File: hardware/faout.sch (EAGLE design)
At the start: 124 parts, among them IC1 MT48LC64M4A2, Q1 12MHz, Q2 ASFL, U1 93C46B, U10 OPA2277UA/2K5E4, U11 DAC8811DGK, U12 MCP1700T-2502E/TT, U13 AD7980ARMZ, U14 ADR435ARZ, U15 AD8627AKSZ-R2, U2 LTC3419EMS, U3 FLASH-SPI-25XXSMD1, U4 6SLX9TQG144, U5 AD8220ARMZ, U6 REF102AU, U7 OPA2277UA/2K5E4, U8 DAC8811DGK, U9 REF102AU

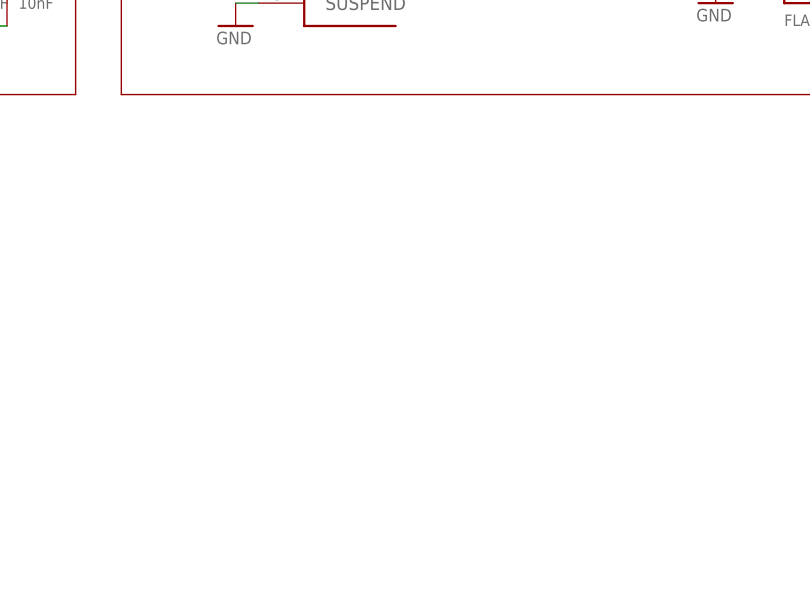
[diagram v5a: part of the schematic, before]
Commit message: Added 7-segment display.
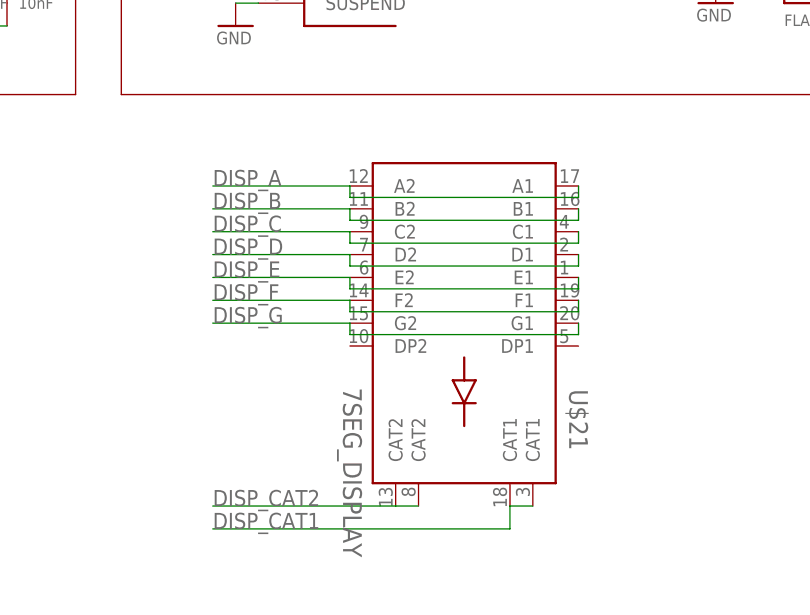
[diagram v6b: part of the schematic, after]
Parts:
- added U$21: 7SEG_DISPLAY, faout:7SEG_DISPLAY
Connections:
- new net DISP_A: U$21.A1, U$21.A2
- new net DISP_B: U$21.B1, U$21.B2
- new net DISP_C: U$21.C1, U$21.C2
- new net DISP_CAT1: U$21.CAT1@1, U$21.CAT1@2
- new net DISP_CAT2: U$21.CAT2@1, U$21.CAT2@2
- new net DISP_D: U$21.D1, U$21.D2
- new net DISP_E: U$21.E1, U$21.E2
- new net DISP_F: U$21.F1, U$21.F2
- new net DISP_G: U$21.G1, U$21.G2
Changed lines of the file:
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@@
 <part name="JP3" library="pinhead" deviceset="PINHD-1X2" device=""/>
 <part name="GND_PWR62" library="faout" deviceset="GND" device=""/>
+<part name="U$21" library="faout" deviceset="7SEG_DISPLAY" device=""/>
 </parts>
 <sheets>
@@
 <instance part="JP3" gate="G$1" x="55.88" y="-139.7"/>
 <instance part="GND_PWR62" gate="A" x="53.34" y="-142.24"/>
+<instance part="U$21" gate="G$1" x="182.88" y="-320.04" rot="R270"/>
 </instances>
 <busses>
@@
 </segment>
 </net>
+<net name="DISP_A" class="0">
+<segment>
+<pinref part="U$21" gate="G$1" pin="A1"/>
+<wire x1="195.58" y1="-307.34" x2="195.58" y2="-308.61" width="0.1524" layer="91"/>
+<wire x1="195.58" y1="-308.61" x2="170.18" y2="-308.61" width="0.1524" layer="91"/>
+<pinref part="U$21" gate="G$1" pin="A2"/>
+<wire x1="170.18" y1="-308.61" x2="170.18" y2="-307.34" width="0.1524" layer="91"/>
+<wire x1="154.94" y1="-307.34" x2="170.18" y2="-307.34" width="0.1524" layer="91"/>
+<label x="154.94" y="-307.34" size="1.778" layer="95"/>
+</segment>
+</net>
+<net name="DISP_B" class="0">
+<segment>
+<pinref part="U$21" gate="G$1" pin="B2"/>
+<wire x1="170.18" y1="-309.88" x2="170.18" y2="-311.15" width="0.1524" layer="91"/>
+<wire x1="170.18" y1="-311.15" x2="195.58" y2="-311.15" width="0.1524" layer="91"/>
+<pinref part="U$21" gate="G$1" pin="B1"/>
+<wire x1="195.58" y1="-311.15" x2="195.58" y2="-309.88" width="0.1524" layer="91"/>
+<wire x1="170.18" y1="-309.88" x2="154.94" y2="-309.88" width="0.1524" layer="91"/>
+<label x="154.94" y="-309.88" size="1.778" layer="95"/>
+</segment>
+</net>
+<net name="DISP_C" class="0">
+<segment>
+<pinref part="U$21" gate="G$1" pin="C1"/>
+<wire x1="195.58" y1="-312.42" x2="195.58" y2="-313.69" width="0.1524" layer="91"/>
+<wire x1="195.58" y1="-313.69" x2="170.18" y2="-313.69" width="0.1524" layer="91"/>
+<pinref part="U$21" gate="G$1" pin="C2"/>
+<wire x1="170.18" y1="-313.69" x2="170.18" y2="-312.42" width="0.1524" layer="91"/>
+<wire x1="170.18" y1="-312.42" x2="154.94" y2="-312.42" width="0.1524" layer="91"/>
+<label x="154.94" y="-312.42" size="1.778" layer="95"/>
+</segment>
+</net>
+<net name="DISP_D" class="0">
+<segment>
+<pinref part="U$21" gate="G$1" pin="D2"/>
+<wire x1="170.18" y1="-314.96" x2="170.18" y2="-316.23" width="0.1524" layer="91"/>
+<wire x1="170.18" y1="-316.23" x2="195.58" y2="-316.23" width="0.1524" layer="91"/>
+<pinref part="U$21" gate="G$1" pin="D1"/>
+<wire x1="195.58" y1="-316.23" x2="195.58" y2="-314.96" width="0.1524" layer="91"/>
+<wire x1="170.18" y1="-314.96" x2="154.94" y2="-314.96" width="0.1524" layer="91"/>
+<label x="154.94" y="-314.96" size="1.778" layer="95"/>
+</segment>
+</net>
+<net name="DISP_E" class="0">
+<segment>
+<pinref part="U$21" gate="G$1" pin="E1"/>
+<wire x1="195.58" y1="-317.5" x2="195.58" y2="-318.77" width="0.1524" layer="91"/>
+<wire x1="195.58" y1="-318.77" x2="170.18" y2="-318.77" width="0.1524" layer="91"/>
+<pinref part="U$21" gate="G$1" pin="E2"/>
+<wire x1="170.18" y1="-318.77" x2="170.18" y2="-317.5" width="0.1524" layer="91"/>
+<wire x1="170.18" y1="-317.5" x2="154.94" y2="-317.5" width="0.1524" layer="91"/>
+<label x="154.94" y="-317.5" size="1.778" layer="95"/>
+</segment>
+</net>
+<net name="DISP_F" class="0">
+<segment>
+<pinref part="U$21" gate="G$1" pin="F2"/>
+<wire x1="170.18" y1="-320.04" x2="170.18" y2="-321.31" width="0.1524" layer="91"/>
+<wire x1="170.18" y1="-321.31" x2="195.58" y2="-321.31" width="0.1524" layer="91"/>
+<pinref part="U$21" gate="G$1" pin="F1"/>
+<wire x1="195.58" y1="-321.31" x2="195.58" y2="-320.04" width="0.1524" layer="91"/>
+<wire x1="170.18" y1="-320.04" x2="154.94" y2="-320.04" width="0.1524" layer="91"/>
+<label x="154.94" y="-320.04" size="1.778" layer="95"/>
+</segment>
+</net>
+<net name="DISP_G" class="0">
+<segment>
+<pinref part="U$21" gate="G$1" pin="G2"/>
+<wire x1="170.18" y1="-322.58" x2="170.18" y2="-323.85" width="0.1524" layer="91"/>
+<wire x1="170.18" y1="-323.85" x2="195.58" y2="-323.85" width="0.1524" layer="91"/>
+<pinref part="U$21" gate="G$1" pin="G1"/>
+<wire x1="195.58" y1="-323.85" x2="195.58" y2="-322.58" width="0.1524" layer="91"/>
+<wire x1="170.18" y1="-322.58" x2="154.94" y2="-322.58" width="0.1524" layer="91"/>
+<label x="154.94" y="-322.58" size="1.778" layer="95"/>
+</segment>
+</net>
+<net name="DISP_CAT2" class="0">
+<segment>
+<pinref part="U$21" gate="G$1" pin="CAT2@1"/>
+<pinref part="U$21" gate="G$1" pin="CAT2@2"/>
+<wire x1="177.8" y1="-342.9" x2="175.26" y2="-342.9" width="0.1524" layer="91"/>
+<wire x1="175.26" y1="-342.9" x2="154.94" y2="-342.9" width="0.1524" layer="91"/>
+<label x="154.94" y="-342.9" size="1.778" layer="95"/>
+</segment>
+</net>
+<net name="DISP_CAT1" class="0">
+<segment>
+<pinref part="U$21" gate="G$1" pin="CAT1@1"/>
+<pinref part="U$21" gate="G$1" pin="CAT1@2"/>
+<wire x1="190.5" y1="-342.9" x2="187.96" y2="-342.9" width="0.1524" layer="91"/>
+<wire x1="187.96" y1="-342.9" x2="187.96" y2="-345.44" width="0.1524" layer="91"/>
+<wire x1="187.96" y1="-345.44" x2="154.94" y2="-345.44" width="0.1524" layer="91"/>
+<label x="154.94" y="-345.44" size="1.778" layer="95"/>
+</segment>
+</net>

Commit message: Finished User IO, create new power supply.
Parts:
- removed R10, R12, R9: 1K5 1%, faout:R_EU0603
- removed R11: 6K8 1%, faout:R_EU0603
- removed U$21: 7SEG_DISPLAY, faout:7SEG_DISPLAY
- added C72, C73, C74: 4.7uF, faout:C_EU0603
- added DISP1: 7SEG_DISPLAY, faout:7SEG_DISPLAY
- added JP4: (no value), pinhead:PINHD-1X6
- added LED3, LED4, LED5: (no value), led:LEDSML0805
- added Q3: MUN2214T1, transistor-npn:MUN2214T1
- added Q4: ASFL, crystal:ASFL
- added R21, R22, R23: 10k, faout:R_EU0603
- added R24, R25, R26, R27, R28: 300, faout:R_EU0603
- added R29, R30: 7.47k, faout:R_EU0603
- added R31: 134k, faout:R_EU0603
- added R32, R33: 2k, faout:R_EU0603
- added SW1, SW2, SW3: SMD_TACT_SWITCH, faout:SMD_TACT_SWITCH
- added U16: LM3671MF-3.3, faout:LM3671MF-3.3
- C1, C19, C20, C28, C29, C30, C31, C34, C36, C38, C4, C40, C41, C42, C43, C46, C48, C49, C6: OC_FARNELL (none) -> 1833803
- C10, C11, C13, C14, C15, C16, C5, C51, C53, C61, C62, C66, C67, C68, C7, C8, C9: OC_FARNELL (none) -> 1740621
- C12: value 10uF/10V -> 4.7uF; device faout:C_EU0805 -> faout:C_EU0603; OC_FARNELL (none) -> 1833803
- C17, C18, C25, C26, C27, C32, C33, C37, C39, C45, C47: OC_FARNELL (none) -> 1867949
- C22, C23: value 22uF/6V3 -> 4.7uF; device faout:C_EU0805 -> faout:C_EU0603; OC_FARNELL (none) -> 1833803
- C50: value 1uF? -> 100nF; OC_FARNELL (none) -> 1740621
- C54: value 1uF -> 1uF?
- C55: value 1uF -> 100nF; OC_FARNELL (none) -> 1740621
- C56: value 100nF -> 114pF
- C57: value 20pF -> 11.4pF
- C58: value 20pF -> 100nF; OC_FARNELL (none) -> 1740621
- C59, C60: value 1nF -> 20pF
- C63, C64: value 100nF -> 1nF
- C65: value 22uF -> 100nF; device resistor:C-EUC1206 -> faout:C_EU0603; OC_FARNELL (none) -> 1740621
- C69: value 100nF -> 1uF
- C70: value 114pF -> 22uF; device faout:C_EU0603 -> resistor:C-EUC1206
- C71: value 11.4pF -> 1uF
- IC1: value MT48LC64M4A2 -> (none); device faout:MT48LC64M4A2 -> ftdichip-3:FT2232HL
- IC2: value (none) -> MT48LC8M16A2; device ftdichip-3:FT2232HL -> faout:MT48LC8M16A2
- JP1: device pinhead:PINHD-1X6 -> pinhead:PINHD-1X2
- JP2: device pinhead:PINHD-1X2 -> pinhead:PINHD-1X6
- L3: value 3.3uH -> (none); device Bogdan_Commons:L_VLS3015 -> faout:R_EU0603
- L4: value 3.3uH -> 2.2uH; device Bogdan_Commons:L_VLS3015 -> rcl:L-EUL5038P; OC_FARNELL (none) -> 2145272
- L5: value (none) -> 2.2uH; device faout:R_EU0603 -> rcl:L-EUL5038P; OC_FARNELL (none) -> 2145272
- Q2: value ASFL -> MUN2214T1; device crystal:ASFL -> transistor-npn:MUN2214T1; OC_FARNELL (none) -> 2317629
- R14, R15: value 300 -> 100
- R16, R17: value 2k -> 100
- R18, R19: value 7.47k -> 100
- R20: value 134k -> 100
- U10: value OPA2277UA/2K5E4 -> ADR435ARZ; device faout:OPA2277UA/2K5E4 -> faout:ADR435ARZ
- U11: value DAC8811DGK -> AD8627AKSZ-R2; device faout:DAC8811DGK -> faout:AD8627AKSZ-R2
- U12: value MCP1700T-2502E/TT -> OPA2277UA/2K5E4; device faout:MCP1700T-2502E/TT -> faout:OPA2277UA/2K5E4
- U13: value AD7980ARMZ -> OPA2277UA/2K5E4; device faout:AD7980ARMZ -> faout:OPA2277UA/2K5E4
- U14: value ADR435ARZ -> MCP1700T-2502E/TT; device faout:ADR435ARZ -> faout:MCP1700T-2502E/TT
- U15: value AD8627AKSZ-R2 -> AD7980ARMZ; device faout:AD8627AKSZ-R2 -> faout:AD7980ARMZ
- U2: value LTC3419EMS -> LM3671MF-1.2; device Bogdan_Commons:LTC3419EMS -> faout:LM3671MF-1.2
- U7: value OPA2277UA/2K5E4 -> DAC8811DGK; device faout:OPA2277UA/2K5E4 -> faout:DAC8811DGK
- U8: value DAC8811DGK -> REF102AU; device faout:DAC8811DGK -> faout:REF102AU
- U9: value REF102AU -> DAC8811DGK; device faout:REF102AU -> faout:DAC8811DGK
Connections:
- removed net DISP_CAT2: U$21.CAT2@1, U$21.CAT2@2
- removed net FB_1V2: R10.P$2, R12.P$1, U2.VFB2
- removed net FB_3V3: R11.P$1, R9.P$2, U2.VFB1
- removed net LED_1: LED1.A, U4B0.IO_L66P_SCP1_0
- removed net LED_2: LED2.A, U4B0.IO_L66N_SCP0_0
- removed net RAM_A12: IC1G$1.A12, U4B3.IO_L1N_VREF_3
- removed net SW_1V2: L4.1, U2.SW2
- removed net SW_3V3: L3.1, U2.SW1
- new net BUTTON1: SW1.1, U4B2.IO_L12N_D2_MISO3_2
- new net BUTTON2: SW2.1, U4B2.IO_L12P_D1_MISO2_2
- new net BUTTON3: SW3.1, U4B2.IO_L2N_CMPMOSI_2
- new net DISP_EN1: Q3.B, U4B2.IO_L14P_D11_2
- new net DISP_EN2: Q2.B, U4B2.IO_L13N_D10_2
- new net DISP_INT_A: DISP1.A1, DISP1.A2, R14.P$1
- new net DISP_INT_B: DISP1.B1, DISP1.B2, R15.P$1
- new net DISP_INT_C: DISP1.C1, DISP1.C2, R16.P$1
- new net DISP_INT_D: DISP1.D1, DISP1.D2, R17.P$1
- new net DISP_INT_E: DISP1.E1, DISP1.E2, R18.P$1
- new net DISP_INT_F: DISP1.F1, DISP1.F2, R19.P$1
- new net DISP_INT_G: DISP1.G1, DISP1.G2, R20.P$1
- new net JP_1: JP4.1, U4B1.IO_L43N_GCLK4_1
- new net JP_2: JP4.2, U4B1.IO_L45P_1
- new net JP_3: JP4.3, U4B1.IO_L45N_1
- new net JP_4: JP4.4, U4B1.IO_L46P_1
- new net LED1: LED1.A, U4B1.IO_L46N_1
- new net LED2: LED2.A, U4B1.IO_L47P_1
- new net LED3: LED3.A, U4B1.IO_L47N_1
- new net LED_4: LED4.A, U4B0.IO_L66P_SCP1_0
- new net LED_5: LED5.A, U4B0.IO_L66N_SCP0_0
- new net N$17: DISP1.CAT2@1, DISP1.CAT2@2, Q2.C
- new net N$18: R21.P$1, SW1.2
- new net N$19: R22.P$1, SW2.2
- new net N$20: R23.P$1, SW3.2
- new net N$21: LED1.C, R24.P$2
- new net N$22: LED2.C, R25.P$2
- new net N$23: LED3.C, R26.P$2
- new net N$24: L4.1, U16.SW
- new net N$25: L5.1, U2.SW
- net !DAC1_CS: now also U7.!CS; no longer U8.!CS
- net !DAC2_CS: now also U9.!CS; no longer U11.!CS
- net !RAM_CAS: now also IC2G$1.!CAS; no longer IC1G$1.!CAS
- net !RAM_RAS: now also IC2G$1.!RAS; no longer IC1G$1.!RAS
- net !RAM_WE: now also IC2G$1.!WE; no longer IC1G$1.!WE
- net !USB_OE: now also IC1.ACBUS6; no longer IC2.ACBUS6
- net !USB_RD: now also IC1.ACBUS2; no longer IC2.ACBUS2
- net !USB_RESET: now also IC1.-RESET, JP1.1; no longer IC2.-RESET, JP3.1
- net !USB_RXF: now also IC1.ACBUS0; no longer IC2.ACBUS0
- net !USB_TXE: now also IC1.ACBUS1; no longer IC2.ACBUS1
- net !USB_WR: now also IC1.ACBUS3; no longer IC2.ACBUS3
- net 1V2: now also C73.P$1, C74.P$1, L5.2, U2.FB; no longer C23.P$1, L4.2, R12.P$2
- net 1V8: now also IC1.VCORE@1, IC1.VCORE@2, IC1.VCORE@3, IC1.VREGOUT; no longer IC2.VCORE@1, IC2.VCORE@2, IC2.VCORE@3, IC2.VREGOUT
- net 2V5: now also C69.P$1, U14.VOUT, U15.VDD; no longer C55.P$1, U12.VOUT, U13.VDD
- net 3V3: now also C23.P$1, C72.P$1, IC1.ACBUS4, IC1.VCCIO@1, IC1.VCCIO@2, IC1.VCCIO@3, IC1.VCCIO@4, IC1.VREGIN, IC2P.VDD@1, IC2P.VDD@2, IC2P.VDD@3, IC2P.VDDQ@1, IC2P.VDDQ@2, IC2P.VDDQ@3, IC2P.VDDQ@4, JP2.6, JP4.6, L3.P$1, L4.2, Q4.OE, Q4.VCC, R21.P$2, R22.P$2, R23.P$2, U16.FB, U2.EN; no longer C22.P$1, IC1P.VDD@1, IC1P.VDD@2, IC1P.VDD@3, IC1P.VDDQ@1, IC1P.VDDQ@2, IC1P.VDDQ@3, IC1P.VDDQ@4, IC2.ACBUS4, IC2.VCCIO@1, IC2.VCCIO@2, IC2.VCCIO@3, IC2.VCCIO@4, IC2.VREGIN, JP1.6, L1.P$1, L3.2, Q2.OE, Q2.VCC, R11.P$2, U2.RUN2
- net 5V0: now also C22.P$1, U16.EN, U16.VIN; no longer U2.MODE, U2.RUN1
- net A+12V: now also C50.P$1, C58.P$1, C65.P$1, C67.P$1, U10.VIN, U11.V+, U12.V+, U13.V+; no longer C56.P$1, C63.P$1, C66.P$1, C68.P$1, U10.V+, U14.VIN, U15.V+, U7.V+
- net A+3V3: now also C55.P$1, C71.P$1, U14.VIN, U15.VIO, U7.VDD, U8.V+, U9.VDD; no longer C50.P$1, C51.P$1, U11.VDD, U12.VIN, U13.VIO, U8.VDD, U9.V+
- net A-12V: now also C51.P$2, C66.P$2, C68.P$2, U11.V-, U12.V-, U13.V-; no longer C64.P$2, C67.P$2, C69.P$2, U10.V-, U15.V-, U7.V-
- net ADC1_CNV: now also U15.CNV; no longer U13.CNV
- net ADC1_REF: now also C70.1, U10.VOUT, U15.REF; no longer C65.1, U13.REF, U14.VOUT
- net ADC1_SCK: now also U15.SCK; no longer U13.SCK
- net ADC1_SDI: now also U15.SDI; no longer U13.SDI
- net ADC1_SDO: now also U15.SDO; no longer U13.SDO
- net CLK_IN: now also Q4.FO; no longer Q2.FO
- net DAC1_CLK: now also U7.CLK; no longer U8.CLK
- net DAC1_IOUT: now also C59.P$2, U13.-IN_A, U7.IOUT; no longer C57.P$2, U7.-IN_A, U8.IOUT
- net DAC1_SDI: now also U7.SDI; no longer U8.SDI
- net DAC1_VOUT: now also C59.P$1, U13.OUT_A, U7.RFB; no longer C57.P$1, U7.OUT_A, U8.RFB
- net DAC1_VREF: now also C52.P$2, C63.P$2, U13.OUT_B, U7.VREF; no longer C50.P$2, C59.P$2, U7.OUT_B, U8.VREF
- net DAC1_VREFOUT: now also C63.P$1, R32.P$2, U13.-IN_B; no longer C59.P$1, R16.P$2, U7.-IN_B
- net DAC2_CLK: now also U9.CLK; no longer U11.CLK
- net DAC2_IOUT: now also C60.P$2, U12.-IN_A, U9.IOUT; no longer C58.P$2, U10.-IN_A, U11.IOUT
- net DAC2_SDI: now also U9.SDI; no longer U11.SDI
- net DAC2_VOUT: now also C60.P$1, U12.OUT_A, U9.RFB; no longer C58.P$1, U10.OUT_A, U11.RFB
- net DAC2_VREF: now also C54.P$2, C64.P$2, U12.OUT_B, U8.COM, U9.VREF; no longer C52.P$2, C60.P$2, U10.OUT_B, U11.VREF, U9.COM
- net DAC2_VREFOUT: now also C64.P$1, R33.P$2, U12.-IN_B; no longer C60.P$1, R17.P$2, U10.-IN_B
- net DISP_A: now also R14.P$2, U4B2.IO_L30N_GCLK0_USERCCLK_2; no longer U$21.A1, U$21.A2
- net DISP_B: now also R15.P$2, U4B2.IO_L30P_GCLK1_D13_2; no longer U$21.B1, U$21.B2
- net DISP_C: now also R16.P$2, U4B2.IO_L48P_D7_2; no longer U$21.C1, U$21.C2
- net DISP_CAT1: now also DISP1.CAT1@1, DISP1.CAT1@2, Q3.C; no longer U$21.CAT1@1, U$21.CAT1@2
- net DISP_D: now also R17.P$2, U4B2.IO_L31N_GCLK30_D15_2; no longer U$21.D1, U$21.D2
- net DISP_E: now also R18.P$2, U4B2.IO_L48N_RDWR_B_VREF_2; no longer U$21.E1, U$21.E2
- net DISP_F: now also R19.P$2, U4B2.IO_L31P_GCLK31_D14_2; no longer U$21.F1, U$21.F2
- net DISP_G: now also R20.P$2, U4B2.IO_L14N_D12_2; no longer U$21.G1, U$21.G2
- net EECS: now also IC1.EECS; no longer IC2.EECS
- net EEDATA: now also IC1.EEDATA; no longer IC2.EEDATA
- net EESK: now also IC1.EESK; no longer IC2.EESK
- net GND: now also C50.P$2, C51.P$1, C57.P$2, C58.P$2, C65.P$2, C66.P$1, C67.P$2, C68.P$1, C69.P$2, C70.2, C72.P$2, C73.P$2, C74.P$2, IC1.AGND, IC1.GND@1, IC1.GND@2, IC1.GND@3, IC1.GND@4, IC1.GND@5, IC1.GND@6, IC1.GND@7, IC1.GND@8, IC1.TEST, IC2P.VSS@1, IC2P.VSS@2, IC2P.VSS@3, IC2P.VSSQ@1, IC2P.VSSQ@2, IC2P.VSSQ@3, IC2P.VSSQ@4, JP1.2, JP2.1, JP4.5, L1.P$2, Q2.E, Q3.E, Q4.GND, R24.P$1, R25.P$1, R26.P$1, R27.P$1, R28.P$1, R30.P$1, SW1.3, SW1.4, SW2.3, SW2.4, SW3.3, SW3.4, U10.GND, U12.+IN_A, U12.+IN_B, U13.+IN_A, U13.+IN_B, U15.GND, U15.IN-, U16.GND, U2.GND, U7.GND, U9.GND; no longer C51.P$2, C54.P$2, C56.P$2, C63.P$2, C64.P$1, C65.2, C66.P$2, C67.P$1, C68.P$2, C69.P$1, IC1P.VSS@1, IC1P.VSS@2, IC1P.VSS@3, IC1P.VSSQ@1, IC1P.VSSQ@2, IC1P.VSSQ@3, IC1P.VSSQ@4, IC2.AGND, IC2.GND@1, IC2.GND@2, IC2.GND@3, IC2.GND@4, IC2.GND@5, IC2.GND@6, IC2.GND@7, IC2.GND@8, IC2.TEST, JP1.1, JP2.2, L5.P$2, Q2.GND, R10.P$1, R14.P$1, R15.P$1, R19.P$1, R9.P$1, U10.+IN_A, U10.+IN_B, U11.GND, U12.GND, U13.GND, U13.IN-, U2.GND@5, U2.GND@6, U7.+IN_A, U7.+IN_B, U8.GND
- net N$1: now also IC1.XTIN; no longer IC2.XTIN
- net N$10: now also R32.P$1; no longer R16.P$1
- net N$12: now also C56.P$1, U11.-IN, U11.OUT_A, U15.IN+; no longer C70.P$1, U13.IN+, U15.-IN, U15.OUT_A
- net N$13: now also R29.P$2; no longer R18.P$2
- net N$14: now also C56.P$2, R29.P$1, R30.P$2, R31.P$1; no longer C70.P$2, R18.P$1, R19.P$2, R20.P$1
- net N$15: now also C57.P$1, R31.P$2, U11.+IN; no longer C71.P$1, R20.P$2, U15.+IN
- net N$16: now also L1.P$1; no longer L5.P$1
- net N$2: now also IC1.XTOUT; no longer IC2.XTOUT
- net N$3: now also LED4.C, R27.P$2; no longer LED1.C, R14.P$2
- net N$4: now also LED5.C, R28.P$2; no longer LED2.C, R15.P$2
- net N$5: now also IC1.VPHY, L3.P$2; no longer IC2.VPHY, L2.P$2
- net N$7: now also IC1.VPLL, L2.P$2; no longer IC2.VPLL, L1.P$2
- net N$8: now also R33.P$1, U8.VOUT; no longer R17.P$1, U9.VOUT
- net RAM_A0: now also IC2G$1.A0; no longer IC1G$1.A0
- net RAM_A1: now also IC2G$1.A1; no longer IC1G$1.A1
- net RAM_A10: now also IC2G$1.A10; no longer IC1G$1.A10
- net RAM_A11: now also IC2G$1.A11; no longer IC1G$1.A11
- net RAM_A2: now also IC2G$1.A2; no longer IC1G$1.A2
- net RAM_A3: now also IC2G$1.A3; no longer IC1G$1.A3
- net RAM_A4: now also IC2G$1.A4; no longer IC1G$1.A4
- net RAM_A5: now also IC2G$1.A5; no longer IC1G$1.A5
- net RAM_A6: now also IC2G$1.A6; no longer IC1G$1.A6
- net RAM_A7: now also IC2G$1.A7; no longer IC1G$1.A7
- net RAM_A8: now also IC2G$1.A8; no longer IC1G$1.A8
- net RAM_A9: now also IC2G$1.A9; no longer IC1G$1.A9
- net RAM_BA0: now also IC2G$1.BA0; no longer IC1G$1.BA0
- net RAM_BA1: now also IC2G$1.BA1; no longer IC1G$1.BA1
- net RAM_CKE: now also IC2G$1.CKE; no longer IC1G$1.CKE
- net RAM_CLK: now also IC2G$1.CLK; no longer IC1G$1.CLK
- net RAM_CS: now also IC2G$1.\CS; no longer IC1G$1.\CS
- net RAM_DQ0: now also IC2G$1.DQ0; no longer IC1G$1.DQ0
- net RAM_DQ1: now also IC2G$1.DQ1; no longer IC1G$1.DQ1
- net RAM_DQ10: now also IC2G$1.DQ10; no longer IC1G$1.DQ10
- net RAM_DQ11: now also IC2G$1.DQ11; no longer IC1G$1.DQ11
- net RAM_DQ12: now also IC2G$1.DQ12; no longer IC1G$1.DQ12
- net RAM_DQ13: now also IC2G$1.DQ13; no longer IC1G$1.DQ13
- net RAM_DQ14: now also IC2G$1.DQ14; no longer IC1G$1.DQ14
- net RAM_DQ15: now also IC2G$1.DQ15; no longer IC1G$1.DQ15
- net RAM_DQ2: now also IC2G$1.DQ2; no longer IC1G$1.DQ2
- net RAM_DQ3: now also IC2G$1.DQ3; no longer IC1G$1.DQ3
- net RAM_DQ4: now also IC2G$1.DQ4; no longer IC1G$1.DQ4
- net RAM_DQ5: now also IC2G$1.DQ5; no longer IC1G$1.DQ5
- net RAM_DQ6: now also IC2G$1.DQ6; no longer IC1G$1.DQ6
- net RAM_DQ7: now also IC2G$1.DQ7; no longer IC1G$1.DQ7
- net RAM_DQ8: now also IC2G$1.DQ8; no longer IC1G$1.DQ8
- net RAM_DQ9: now also IC2G$1.DQ9; no longer IC1G$1.DQ9
- net RAM_DQMH: now also IC2G$1.DQMH; no longer IC1G$1.DQMH
- net RAM_DQML: now also IC2G$1.DQML; no longer IC1G$1.DQML
- net RESET: now also JP3.1; no longer JP2.1
- net TCK: now also IC1.BDBUS0, JP2.2; no longer IC2.BDBUS0, JP1.2
- net TDI: now also IC1.BDBUS1, JP2.3; no longer IC2.BDBUS1, JP1.3
- net TDO: now also IC1.BDBUS2, JP2.4; no longer IC2.BDBUS2, JP1.4
- net TMS: now also IC1.BDBUS3, JP2.5; no longer IC2.BDBUS3, JP1.5
- net USB_CLKOUT: now also IC1.ACBUS5; no longer IC2.ACBUS5
- net USB_D0: now also IC1.ADBUS0; no longer IC2.ADBUS0
- net USB_D1: now also IC1.ADBUS1; no longer IC2.ADBUS1
- net USB_D2: now also IC1.ADBUS2; no longer IC2.ADBUS2
- net USB_D3: now also IC1.ADBUS3; no longer IC2.ADBUS3
- net USB_D4: now also IC1.ADBUS4; no longer IC2.ADBUS4
- net USB_D5: now also IC1.ADBUS5; no longer IC2.ADBUS5
- net USB_D6: now also IC1.ADBUS6; no longer IC2.ADBUS6
- net USB_D7: now also IC1.ADBUS7; no longer IC2.ADBUS7
- net USB_DM: now also IC1.D-; no longer IC2.D-
- net USB_DP: now also IC1.D+; no longer IC2.D+
- net USB_REF: now also IC1.REF; no longer IC2.REF
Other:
- note added: "FPGA User IO"
- moved on the sheet: AI1, C12, C22, C23, C25, C26, C27, C28, C29, C30, C31, C32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

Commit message: Finalize design.
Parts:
- removed R30: 7.47k, faout:R_EU0603
- removed R31: 134k, faout:R_EU0603
- removed R32, R33: 2k, faout:R_EU0603
- added C75: 20pF, faout:C_EU0603
- added C76, C77, C80, C81, C82, C83: 100nF, faout:C_EU0603
- added C78, C79: 1nF, faout:C_EU0603
- added C84, C86: 1uF, faout:C_EU0603
- added C85: 22uF, resistor:C-EUC1206
- added JP5: (no value), pinhead:PINHD-1X6
- added Q5: ASFL, crystal:ASFL
- added R10, R11, R12: 100, faout:R_EU0603
- added R9: 4.7k, faout:R_EU0603
- added U17: MCP1700T-2502E/TT, faout:MCP1700T-2502E/TT
- added U18: AD7980ARMZ, faout:AD7980ARMZ
- C1: value 3.3uF -> 10uF; device faout:C_EU0603 -> faout:C_EU0805; OC_FARNELL 1833803 -> 1867958
- C10, C51, C53, C55, C58, C61: value 100nF -> 4.7uF; OC_FARNELL 1740621 -> 1833803
- C11, C13, C14, C15, C8, C9: value 100nF -> 10uF; device faout:C_EU0603 -> faout:C_EU0805; OC_FARNELL 1740621 -> 1867958
- C12: value 4.7uF -> 10uF; device faout:C_EU0603 -> faout:C_EU0805; OC_FARNELL 1833803 -> 1867958
- C17, C25, C26, C27: value 470nF -> 100nF; OC_FARNELL 1867949 -> 1740621
- C18, C32, C33, C45: value 470nF -> 4.7uF; OC_FARNELL 1867949 -> 1833803
- C2: value 18pF -> 10uF; device faout:C_EU0603 -> faout:C_EU0805; OC_FARNELL (none) -> 1867958
- C20, C23, C28, C73: value 4.7uF -> 100nF; OC_FARNELL 1833803 -> 1740621
- C21, C44: value 10nF -> 4.7uF; OC_FARNELL (none) -> 1833803
- C24: value 10nF -> 100nF; OC_FARNELL (none) -> 1740621
- C29, C30, C40, C41, C42, C48: value 4.7uF -> 470nF; OC_FARNELL 1833803 -> 1867949
- C3: value 18pF -> 3.3uF; OC_FARNELL (none) -> 1833803
- C35: value 470nF -> 4.7uF; OC_FARNELL (none) -> 1833803
- C37, C39: value 470nF -> 10nF; OC_FARNELL 1867949 -> (none)
- C38: value 4.7uF -> 100uF; device faout:C_EU0603 -> rcl:CPOL-EUE; OC_FARNELL 1833803 -> 9693467
- C4: value 4.7uF -> 18pF; OC_FARNELL 1833803 -> (none)
- C5: value 100nF -> 18pF; OC_FARNELL 1740621 -> (none)
- C50: value 100nF -> 470nF; OC_FARNELL 1740621 -> (none)
- C52, C54: value 1uF? -> 470nF; OC_FARNELL (none) -> 1867949
- C56: value 114pF -> 4.7uF; OC_FARNELL (none) -> 1833803
- C57: value 11.4pF -> 4.7uF; OC_FARNELL (none) -> 1833803
- C59: value 20pF -> 10nF
- C60: value 20pF -> 470nF; OC_FARNELL (none) -> 1867949
- C62: value 100nF -> 470nF; OC_FARNELL 1740621 -> 1867949
- C63, C64: value 1nF -> 4.7uF; OC_FARNELL (none) -> 1833803
- C67: value 100nF -> 1uF?; OC_FARNELL 1740621 -> (none)
- C69: value 1uF -> 1uF?
- C70: value 22uF -> 100nF; device resistor:C-EUC1206 -> faout:C_EU0603; OC_FARNELL (none) -> 1740621
- C71: value 1uF -> 114pF
- C72: value 4.7uF -> 11.4pF; OC_FARNELL 1833803 -> (none)
- C74: value 4.7uF -> 20pF; OC_FARNELL 1833803 -> (none)
- JP1: device pinhead:PINHD-1X2 -> pinhead:PINHD-1X3
- JP2, JP4: device pinhead:PINHD-1X6 -> pinhead:PINHD-1X2
- JP3: device pinhead:PINHD-1X2 -> pinhead:PINHD-1X6
- Q1: value 12MHz -> L7912ACV; device faout:TXC_QUARTZ_7A -> faout:L7912ACV; OC_FARNELL 1841940 -> (none)
- Q2: value MUN2214T1 -> 12MHz; device transistor-npn:MUN2214T1 -> faout:TXC_QUARTZ_7A; OC_FARNELL 2317629 -> 1841940
- Q4: value ASFL -> MUN2214T1; device crystal:ASFL -> transistor-npn:MUN2214T1; OC_FARNELL (none) -> 2317629
- R13: value 4.7k -> 100
- R17, R18, R19: value 100 -> 10k
- R20: value 100 -> 300
- R21, R22, R23: value 10k -> 300
- R25, R26: value 300 -> 7.47k
- R27: value 300 -> 134k
- R28: value 300 -> 2k
- R29: value 7.47k -> 2k
- U1: value 93C46B -> 93LC46BT-I/OT; device Bogdan_Commons:DIGITAL-EEPROM-MICROWIRE-6P_SOT23 -> faout:93LC46BT-I/OT
- U10: value ADR435ARZ -> DAC8811DGK; device faout:ADR435ARZ -> faout:DAC8811DGK
- U11: value AD8627AKSZ-R2 -> REF102AU; device faout:AD8627AKSZ-R2 -> faout:REF102AU
- U12: value OPA2277UA/2K5E4 -> DAC8811DGK; device faout:OPA2277UA/2K5E4 -> faout:DAC8811DGK
- U13: value OPA2277UA/2K5E4 -> ADR435ARZ; device faout:OPA2277UA/2K5E4 -> faout:ADR435ARZ
- U14: value MCP1700T-2502E/TT -> AD8627AKSZ-R2; device faout:MCP1700T-2502E/TT -> faout:AD8627AKSZ-R2
- U15: value AD7980ARMZ -> OPA2277UA/2K5E4; device faout:AD7980ARMZ -> faout:OPA2277UA/2K5E4
- U16: value LM3671MF-3.3 -> OPA2277UA/2K5E4; device faout:LM3671MF-3.3 -> faout:OPA2277UA/2K5E4
- U2: value LM3671MF-1.2 -> LM3480IM3-3.3; device faout:LM3671MF-1.2 -> faout:LM3480IM3-3.3
- U3: value FLASH-SPI-25XXSMD1 -> LM2940T-12.0; device GadgetFactory:FLASH-SPI-25XXSMD1 -> faout:LM2940T-12.0
- U4: value 6SLX9TQG144 -> LM3671MF-3.3; device faout:6SLX9TQG144 -> faout:LM3671MF-3.3
- U5: value AD8220ARMZ -> LM3671MF-1.2; device faout:AD8220ARMZ -> faout:LM3671MF-1.2
- U6: value REF102AU -> FLASH-SPI-25XXSMD1; device faout:REF102AU -> GadgetFactory:FLASH-SPI-25XXSMD1
- U7: value DAC8811DGK -> 6SLX9TQG144; device faout:DAC8811DGK -> faout:6SLX9TQG144; OC_FARNELL (none) -> 1876228
- U8: value REF102AU -> AD8220ARMZ; device faout:REF102AU -> faout:AD8220ARMZ
- U9: value DAC8811DGK -> REF102AU; device faout:DAC8811DGK -> faout:REF102AU
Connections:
- new net +15V: C1.P$1, JP1.1, U2.IN, U3.IN
- new net -15V: C2.P$1, JP1.2, Q1.IN
- net !DAC1_CS: now also U10.!CS, U7B1.IO_L40N_GCLK10_1; no longer U4B1.IO_L40N_GCLK10_1, U7.!CS
- net !DAC2_CS: now also U12.!CS, U7B1.IO_L42P_GCLK7_1; no longer U4B1.IO_L42P_GCLK7_1, U9.!CS
- net !RAM_CAS: now also U7B3.IO_L52N_3; no longer U4B3.IO_L52N_3
- net !RAM_RAS: now also U7B3.IO_L83P_3; no longer U4B3.IO_L83P_3
- net !RAM_WE: now also U7B3.IO_L52P_3; no longer U4B3.IO_L52P_3
- net !USB_OE: now also U7B0.IO_L64N_SCP4_0; no longer U4B0.IO_L64N_SCP4_0
- net !USB_RD: now also U7B0.IO_L63P_SCP7_0; no longer U4B0.IO_L63P_SCP7_0
- net !USB_RESET: now also JP2.1; no longer JP1.1
- net !USB_RXF: now also U7B0.IO_L62P_0; no longer U4B0.IO_L62P_0
- net !USB_TXE: now also U7B0.IO_L62N_VREF_0; no longer U4B0.IO_L62N_VREF_0
- net !USB_WR: now also U7B0.IO_L63N_SCP6_0; no longer U4B0.IO_L63N_SCP6_0
- net 1V2: now also C33.P$1, C36.P$1, C41.P$1, C43.P$1, C45.P$1, C46.P$1, U5.FB, U7BVCCINT.VCCINT@0, U7BVCCINT.VCCINT@1, U7BVCCINT.VCCINT@2, U7BVCCINT.VCCINT@3, U7BVCCINT.VCCINT@4; no longer C26.P$1, C28.P$1, C30.P$1, C31.P$1, C73.P$1, C74.P$1, U2.FB, U4BVCCINT.VCCINT@0, U4BVCCINT.VCCINT@1, U4BVCCINT.VCCINT@2, U4BVCCINT.VCCINT@3, U4BVCCINT.VCCINT@4
- net 1V8: now also C20.P$1, C23.P$1, C24.P$1, C3.P$1; no longer C1.P$1, C10.P$1, C11.P$1, C9.P$1
- net 2V5: now also C84.P$1, U17.VOUT, U18.VDD; no longer C69.P$1, U14.VOUT, U15.VDD
- net 3V3: now also C26.P$1, C28.P$1, C30.P$1, C31.P$1, C38.+, C50.P$1, C51.P$1, C52.P$1, C53.P$1, C54.P$1, C55.P$1, C56.P$1, C57.P$1, C58.P$1, C59.P$1, C60.P$1, C61.P$1, C62.P$1, C63.P$1, C64.P$1, C7.P$1, JP3.6, JP5.6, Q5.OE, Q5.VCC, R17.P$2, R18.P$2, R19.P$2, R9.P$2, U4.FB, U5.EN, U6.HOLD, U6.VCC, U6.WP, U7B0.VCCO_0@0, U7B0.VCCO_0@1, U7B0.VCCO_0@2, U7B1.VCCO_1@0, U7B1.VCCO_1@1, U7B1.VCCO_1@2, U7B2.IO_L1N_M0_CMPMISO_2, U7B2.VCCO_2@0, U7B2.VCCO_2@1, U7B3.VCCO_3@0, U7B3.VCCO_3@1, U7B3.VCCO_3@2, U7BVCCAUX.VCCAUX@0, U7BVCCAUX.VCCAUX@1, U7BVCCAUX.VCCAUX@2, U7BVCCAUX.VCCAUX@3, U7BVCCAUX.VCCAUX@4; no longer C13.P$1, C14.P$1, C15.P$1, C16.P$1, C17.P$1, C18.P$1, C19.P$1, C20.P$1, C21.P$1, C23.P$1, C24.P$1, C33.P$1, C36.P$1, C38.P$1, C41.P$1, C43.P$1, C45.P$1, C46.P$1, C5.P$1, C72.P$1, JP2.6, JP4.6, Q4.OE, Q4.VCC, R13.P$2, R21.P$2, R22.P$2, R23.P$2, U16.FB, U2.EN, U3.HOLD, U3.VCC, U3.WP, U4B0.VCCO_0@0, U4B0.VCCO_0@1, U4B0.VCCO_0@2, U4B1.VCCO_1@0, U4B1.VCCO_1@1, U4B1.VCCO_1@2, U4B2.IO_L1N_M0_CMPMISO_2, U4B2.VCCO_2@0, U4B2.VCCO_2@1, U4B3.VCCO_3@0, U4B3.VCCO_3@1, U4B3.VCCO_3@2, U4BVCCAUX.VCCAUX@0, U4BVCCAUX.VCCAUX@1, U4BVCCAUX.VCCAUX@2, U4BVCCAUX.VCCAUX@3, U4BVCCAUX.VCCAUX@4
- net 5V0: now also C18.P$1, C19.P$1, C21.P$1, U4.EN, U4.VIN, U5.VIN; no longer C12.P$1, U16.EN, U16.VIN, U2.VIN
- net A+12V: now also C12.P$1, C14.P$1, C73.P$1, C76.P$1, C8.P$1, C80.P$1, C82.P$1, U13.VIN, U14.V+, U15.V+, U16.V+, U3.OUT, U8.+VS; no longer C50.P$1, C58.P$1, C61.P$1, C67.P$1, U10.VIN, U11.V+, U12.V+, U13.V+, U5.+VS
- net A+3V3: now also C11.P$1, C67.P$1, C68.P$1, C69.P$1, C70.P$1, C86.P$1, U10.VDD, U11.V+, U12.VDD, U17.VIN, U18.VIO, U2.OUT, U9.V+; no longer C52.P$1, C53.P$1, C54.P$1, C55.P$1, C71.P$1, U14.VIN, U15.VIO, U6.V+, U7.VDD, U8.V+, U9.VDD
- net A-12V: now also C13.P$2, C15.P$2, C77.P$2, C81.P$2, C83.P$2, C9.P$2, Q1.OUTPUT, U14.V-, U15.V-, U16.V-, U8.-VS; no longer C51.P$2, C62.P$2, C68.P$2, U11.V-, U12.V-, U13.V-, U5.-VS
- net ADC1_CNV: now also U18.CNV, U7B1.IO_L33P_1; no longer U15.CNV, U4B1.IO_L33P_1
- net ADC1_REF: now also C85.1, U13.VOUT, U18.REF; no longer C70.1, U10.VOUT, U15.REF
- net ADC1_SCK: now also U18.SCK, U7B1.IO_L34P_1; no longer U15.SCK, U4B1.IO_L34P_1
- net ADC1_SDI: now also U18.SDI, U7B1.IO_L34N_1; no longer U15.SDI, U4B1.IO_L34N_1
- net ADC1_SDO: now also U18.SDO, U7B1.IO_L33N_1; no longer U15.SDO, U4B1.IO_L33N_1
- net BUTTON1: now also U7B2.IO_L12N_D2_MISO3_2; no longer U4B2.IO_L12N_D2_MISO3_2
- net BUTTON2: now also U7B2.IO_L12P_D1_MISO2_2; no longer U4B2.IO_L12P_D1_MISO2_2
- net BUTTON3: now also U7B2.IO_L2N_CMPMOSI_2; no longer U4B2.IO_L2N_CMPMOSI_2
- net CLK_IN: now also Q5.FO, U7B1.IO_L40P_GCLK11_1; no longer Q4.FO, U4B1.IO_L40P_GCLK11_1
- net DAC1_CLK: now also U10.CLK, U7B1.IO_L41P_GCLK9_IRDY1_1; no longer U4B1.IO_L41P_GCLK9_IRDY1_1, U7.CLK
- net DAC1_IOUT: now also C74.P$2, U10.IOUT, U16.-IN_A; no longer C59.P$2, U13.-IN_A, U7.IOUT
- net DAC1_SDI: now also U10.SDI, U7B1.IO_L41N_GCLK8_1; no longer U4B1.IO_L41N_GCLK8_1, U7.SDI
- net DAC1_VOUT: now also C74.P$1, U10.RFB, U16.OUT_A; no longer C59.P$1, U13.OUT_A, U7.RFB
- net DAC1_VREF: now also C67.P$2, C78.P$2, U10.VREF, U16.OUT_B, U9.COM; no longer C52.P$2, C63.P$2, U13.OUT_B, U6.COM, U7.VREF
- net DAC1_VREFOUT: now also C78.P$1, R28.P$2, U16.-IN_B; no longer C63.P$1, R32.P$2, U13.-IN_B
- net DAC2_CLK: now also U12.CLK, U7B1.IO_L42N_GCLK6_TRDY1_1; no longer U4B1.IO_L42N_GCLK6_TRDY1_1, U9.CLK
- net DAC2_IOUT: now also C75.P$2, U12.IOUT, U15.-IN_A; no longer C60.P$2, U12.-IN_A, U9.IOUT
- net DAC2_SDI: now also U12.SDI, U7B1.IO_L43P_GCLK5_1; no longer U4B1.IO_L43P_GCLK5_1, U9.SDI
- net DAC2_VOUT: now also C75.P$1, U12.RFB, U15.OUT_A; no longer C60.P$1, U12.OUT_A, U9.RFB
- net DAC2_VREF: now also C69.P$2, C79.P$2, U11.COM, U12.VREF, U15.OUT_B; no longer C54.P$2, C64.P$2, U12.OUT_B, U8.COM, U9.VREF
- net DAC2_VREFOUT: now also C79.P$1, R29.P$2, U15.-IN_B; no longer C64.P$1, R33.P$2, U12.-IN_B
- net DISP_A: now also R10.P$2, U7B2.IO_L30N_GCLK0_USERCCLK_2; no longer R14.P$2, U4B2.IO_L30N_GCLK0_USERCCLK_2
- net DISP_B: now also R11.P$2, U7B2.IO_L30P_GCLK1_D13_2; no longer R15.P$2, U4B2.IO_L30P_GCLK1_D13_2
- net DISP_C: now also R12.P$2, U7B2.IO_L48P_D7_2; no longer R16.P$2, U4B2.IO_L48P_D7_2
- net DISP_CAT1: now also Q4.C; no longer Q3.C
- net DISP_D: now also R13.P$2, U7B2.IO_L31N_GCLK30_D15_2; no longer R17.P$2, U4B2.IO_L31N_GCLK30_D15_2
- net DISP_E: now also R14.P$2, U7B2.IO_L48N_RDWR_B_VREF_2; no longer R18.P$2, U4B2.IO_L48N_RDWR_B_VREF_2
- net DISP_EN1: now also Q4.B, U7B2.IO_L14P_D11_2; no longer Q3.B, U4B2.IO_L14P_D11_2
- net DISP_EN2: now also Q3.B, U7B2.IO_L13N_D10_2; no longer Q2.B, U4B2.IO_L13N_D10_2
- net DISP_F: now also R15.P$2, U7B2.IO_L31P_GCLK31_D14_2; no longer R19.P$2, U4B2.IO_L31P_GCLK31_D14_2
- net DISP_G: now also R16.P$2, U7B2.IO_L14N_D12_2; no longer R20.P$2, U4B2.IO_L14N_D12_2
- net DISP_INT_A: now also R10.P$1; no longer R14.P$1
- net DISP_INT_B: now also R11.P$1; no longer R15.P$1
- net DISP_INT_C: now also R12.P$1; no longer R16.P$1
- net DISP_INT_D: now also R13.P$1; no longer R17.P$1
- net DISP_INT_E: now also R14.P$1; no longer R18.P$1
- net DISP_INT_F: now also R15.P$1; no longer R19.P$1
- net DISP_INT_G: now also R16.P$1; no longer R20.P$1
- net FLASH_CS: now also U6.CS, U7B2.IO_L65N_CSO_B_2; no longer U3.CS, U4B2.IO_L65N_CSO_B_2
- net FLASH_MISO: now also U6.MISO, U7B2.IO_L3P_D0_DIN_MISO_MISO1_2; no longer U3.MISO, U4B2.IO_L3P_D0_DIN_MISO_MISO1_2
- net FLASH_MOSI: now also U6.MOSI, U7B2.IO_L3N_MOSI_CSI_B_MISO0_2; no longer U3.MOSI, U4B2.IO_L3N_MOSI_CSI_B_MISO0_2
- net FLASH_SCK: now also U6.SCK, U7B2.IO_L1P_CCLK_2; no longer U3.SCK, U4B2.IO_L1P_CCLK_2
- net GND: now also C13.P$1, C15.P$1, C38.-, C51.P$2, C52.P$2, C54.P$2, C56.P$2, C59.P$2, C60.P$2, C62.P$2, C63.P$2, C64.P$2, C68.P$2, C70.P$2, C76.P$2, C77.P$1, C80.P$2, C81.P$1, C82.P$2, C83.P$1, C84.P$2, C85.2, C86.P$2, C9.P$1, JP1.3, JP2.2, JP3.1, JP4.2, JP5.5, Q1.GND, Q4.E, Q5.GND, R20.P$1, R21.P$1, R22.P$1, R23.P$1, U12.GND, U13.GND, U15.+IN_A, U15.+IN_B, U16.+IN_A, U16.+IN_B, U17.GND, U18.GND, U18.IN-, U4.GND, U5.GND, U6.GND, U7B0.IO_L1P_HSWAPEN_0, U7B2.IO_L13P_M1_2, U7BGND.GND@0, U7BGND.GND@1, U7BGND.GND@10, U7BGND.GND@11, U7BGND.GND@12, U7BGND.GND@2, U7BGND.GND@3, U7BGND.GND@4, U7BGND.GND@5, U7BGND.GND@6, U7BGND.GND@7, U7BGND.GND@8, U7BGND.GND@9, U7BNA.SUSPEND, U8.REF; no longer C13.P$2, C15.P$2, C38.P$2, C51.P$1, C62.P$1, C67.P$2, C68.P$1, C69.P$2, C70.2, C71.P$2, C74.P$2, C9.P$2, JP1.2, JP2.1, JP3.2, JP4.5, Q2.E, Q4.GND, R25.P$1, R27.P$1, R28.P$1, R30.P$1, U12.+IN_A, U12.+IN_B, U13.+IN_A, U13.+IN_B, U14.GND, U15.GND, U15.IN-, U16.GND, U4B0.IO_L1P_HSWAPEN_0, U4B2.IO_L13P_M1_2, U4BGND.GND@0, U4BGND.GND@1, U4BGND.GND@10, U4BGND.GND@11, U4BGND.GND@12, U4BGND.GND@2, U4BGND.GND@3, U4BGND.GND@4, U4BGND.GND@5, U4BGND.GND@6, U4BGND.GND@7, U4BGND.GND@8, U4BGND.GND@9, U4BNA.SUSPEND, U5.REF, U7.GND, U9.GND
- net JP_1: now also JP5.1, U7B1.IO_L43N_GCLK4_1; no longer JP4.1, U4B1.IO_L43N_GCLK4_1
- net JP_2: now also JP5.2, U7B1.IO_L45P_1; no longer JP4.2, U4B1.IO_L45P_1
- net JP_3: now also JP5.3, U7B1.IO_L45N_1; no longer JP4.3, U4B1.IO_L45N_1
- net JP_4: now also JP5.4, U7B1.IO_L46P_1; no longer JP4.4, U4B1.IO_L46P_1
- net LED1: now also U7B1.IO_L46N_1; no longer U4B1.IO_L46N_1
- net LED2: now also U7B1.IO_L47P_1; no longer U4B1.IO_L47P_1
- net LED3: now also U7B1.IO_L47N_1; no longer U4B1.IO_L47N_1
- net LED_4: now also U7B0.IO_L66P_SCP1_0; no longer U4B0.IO_L66P_SCP1_0
- net LED_5: now also U7B0.IO_L66N_SCP0_0; no longer U4B0.IO_L66N_SCP0_0
- net N$1: now also C4.P$1, Q2.P$1; no longer C2.P$1, Q1.P$1
- net N$10: now also R28.P$1, U9.VOUT; no longer R32.P$1, U6.VOUT
- net N$11: now also U8.-IN; no longer U5.-IN
- net N$12: now also C71.P$1, U14.-IN, U14.OUT_A, U18.IN+; no longer C56.P$1, U11.-IN, U11.OUT_A, U15.IN+
- net N$13: now also R25.P$2, U8.VOUT; no longer R29.P$2, U5.VOUT
- net N$14: now also C71.P$2, R25.P$1, R26.P$2, R27.P$1; no longer C56.P$2, R29.P$1, R30.P$2, R31.P$1
- net N$15: now also C72.P$1, R27.P$2, U14.+IN; no longer C57.P$1, R31.P$2, U11.+IN
- net N$17: now also Q3.C; no longer Q2.C
- net N$18: now also R17.P$1; no longer R21.P$1
- net N$19: now also R18.P$1; no longer R22.P$1
- net N$2: now also C5.P$1, Q2.P$2; no longer C3.P$1, Q1.P$2
- net N$20: now also R19.P$1; no longer R23.P$1
- net N$21: now also R20.P$2; no longer R24.P$2
- net N$22: now also R21.P$2; no longer R25.P$2
- net N$23: now also R22.P$2; no longer R26.P$2
- net N$24: now also U4.SW; no longer U16.SW
- net N$25: now also U5.SW; no longer U2.SW
- net N$3: now also R23.P$2; no longer R27.P$2
- net N$4: now also R24.P$2; no longer R28.P$2
- net N$5: now also C16.P$1, C6.P$1; no longer C4.P$1, C7.P$1
- net N$7: now also C10.P$1, C17.P$1; no longer C6.P$1, C8.P$1
- net N$8: now also R29.P$1, U11.VOUT; no longer R33.P$1, U8.VOUT
- net N$9: now also U8.+IN; no longer U5.+IN
- net RAM_A0: now also U7B0.IO_L3P_0; no longer U4B0.IO_L3P_0
- net RAM_A1: now also U7B0.IO_L3N_0; no longer U4B0.IO_L3N_0
- net RAM_A10: now also U7B0.IO_L2N_0; no longer U4B0.IO_L2N_0
- net RAM_A11: now also U7B3.IO_L1P_3; no longer U4B3.IO_L1P_3
- net RAM_A2: now also U7B0.IO_L4P_0; no longer U4B0.IO_L4P_0
- net RAM_A3: now also U7B0.IO_L4N_0; no longer U4B0.IO_L4N_0
- net RAM_A4: now also U7B2.IO_L49P_D3_2; no longer U4B2.IO_L49P_D3_2
- net RAM_A5: now also U7B2.IO_L49N_D4_2; no longer U4B2.IO_L49N_D4_2
- net RAM_A6: now also U7B2.IO_L62P_D5_2; no longer U4B2.IO_L62P_D5_2
- net RAM_A7: now also U7B2.IO_L62N_D6_2; no longer U4B2.IO_L62N_D6_2
- net RAM_A8: now also U7B2.IO_L64P_D8_2; no longer U4B2.IO_L64P_D8_2
- net RAM_A9: now also U7B2.IO_L64N_D9_2; no longer U4B2.IO_L64N_D9_2
- net RAM_BA0: now also U7B0.IO_L1N_VREF_0; no longer U4B0.IO_L1N_VREF_0
- net RAM_BA1: now also U7B0.IO_L2P_0; no longer U4B0.IO_L2P_0
- net RAM_CKE: now also U7B3.IO_L2P_3; no longer U4B3.IO_L2P_3
- net RAM_CLK: now also U7B3.IO_L2N_3; no longer U4B3.IO_L2N_3
- net RAM_CS: now also U7B3.IO_L83N_VREF_3; no longer U4B3.IO_L83N_VREF_3
- net RAM_DQ0: now also U7B3.IO_L50N_3; no longer U4B3.IO_L50N_3
- net RAM_DQ1: now also U7B3.IO_L50P_3; no longer U4B3.IO_L50P_3
- net RAM_DQ10: now also U7B3.IO_L41N_GCLK26_3; no longer U4B3.IO_L41N_GCLK26_3
- net RAM_DQ11: now also U7B3.IO_L41P_GCLK27_3; no longer U4B3.IO_L41P_GCLK27_3
- net RAM_DQ12: now also U7B3.IO_L37N_3; no longer U4B3.IO_L37N_3
- net RAM_DQ13: now also U7B3.IO_L37P_3; no longer U4B3.IO_L37P_3
- net RAM_DQ14: now also U7B3.IO_L36N_3; no longer U4B3.IO_L36N_3
- net RAM_DQ15: now also U7B3.IO_L36P_3; no longer U4B3.IO_L36P_3
- net RAM_DQ2: now also U7B3.IO_L49N_3; no longer U4B3.IO_L49N_3
- net RAM_DQ3: now also U7B3.IO_L49P_3; no longer U4B3.IO_L49P_3
- net RAM_DQ4: now also U7B3.IO_L44N_GCLK20_3; no longer U4B3.IO_L44N_GCLK20_3
- net RAM_DQ5: now also U7B3.IO_L44P_GCLK21_3; no longer U4B3.IO_L44P_GCLK21_3
- net RAM_DQ6: now also U7B3.IO_L43N_GCLK22_IRDY2_3; no longer U4B3.IO_L43N_GCLK22_IRDY2_3
- net RAM_DQ7: now also U7B3.IO_L51P_3; no longer U4B3.IO_L51P_3
- net RAM_DQ8: now also U7B3.IO_L42N_GCLK24_3; no longer U4B3.IO_L42N_GCLK24_3
- net RAM_DQ9: now also U7B3.IO_L42P_GCLK25_TRDY2_3; no longer U4B3.IO_L42P_GCLK25_TRDY2_3
- net RAM_DQMH: now also U7B3.IO_L43P_GCLK23_3; no longer U4B3.IO_L43P_GCLK23_3
- net RAM_DQML: now also U7B3.IO_L51N_3; no longer U4B3.IO_L51N_3
- net RESET: now also JP4.1, R9.P$1, U7B2.PROGRAM_B_2; no longer JP3.1, R13.P$1, U4B2.PROGRAM_B_2
- net TCK: now also JP3.2, U7BNA.TCK; no longer JP2.2, U4BNA.TCK
- net TDI: now also JP3.3, U7BNA.TDI; no longer JP2.3, U4BNA.TDI
- net TDO: now also JP3.4, U7BNA.TDO; no longer JP2.4, U4BNA.TDO
- net TMS: now also JP3.5, U7BNA.TMS; no longer JP2.5, U4BNA.TMS
- net USB_CLKOUT: now also U7B0.IO_L37N_GCLK12_0; no longer U4B0.IO_L37N_GCLK12_0
- net USB_D0: now also U7B0.IO_L64P_SCP5_0; no longer U4B0.IO_L64P_SCP5_0
- net USB_D1: now also U7B0.IO_L34P_GCLK19_0; no longer U4B0.IO_L34P_GCLK19_0
- net USB_D2: now also U7B0.IO_L34N_GCLK18_0; no longer U4B0.IO_L34N_GCLK18_0
- net USB_D3: now also U7B0.IO_L35P_GCLK17_0; no longer U4B0.IO_L35P_GCLK17_0
- net USB_D4: now also U7B0.IO_L35N_GCLK16_0; no longer U4B0.IO_L35N_GCLK16_0
- net USB_D5: now also U7B0.IO_L36P_GCLK15_0; no longer U4B0.IO_L36P_GCLK15_0
- net USB_D6: now also U7B0.IO_L36N_GCLK14_0; no longer U4B0.IO_L36N_GCLK14_0
- net USB_D7: now also U7B0.IO_L37P_GCLK13_0; no longer U4B0.IO_L37P_GCLK13_0
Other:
- note added: "Power - Analog"
- moved on the sheet: C1, C10, C11, C12, C13, C14, C15, C16, C17, C18, C19, C2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
